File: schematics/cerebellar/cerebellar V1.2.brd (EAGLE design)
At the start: 95.7 x 90.5 mm, 74 parts, among them CON1 ODRV2, CON2 ODRV1, CON3 ODRV3, CON4 ODRV4, CON5 ODRV5, CON6 ODRV6, IC3 LTC7001, K1 PIN20X2, P1 Foot1, P11 Foot2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

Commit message: restart ODrive
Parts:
- U$6: device TS2509:TSSOP-8 -> TS2509:SO08
- moved U2 2.54 mm to (22.5, 52.1)
- moved IC3 2.27 mm to (35.7, 52.1)
- moved R15 2.27 mm to (47.1, 52.1)
- moved R4 2.27 mm to (44.6, 52.1)
- moved R9 2.27 mm to (49.7, 52.1)
- moved C19 2.27 mm to (31.9, 52.1)
- moved R5 2.27 mm to (26.2, 52.1)
- moved R10 2.27 mm to (42.0, 52.1)
- moved R2 2.27 mm to (28.7, 52.1)
- moved R7 2.27 mm to (39.5, 52.1)
- moved C1 2.17 mm to (54.6, 52.1)
- moved R6 2.09 mm to (52.1, 52.1)
- moved U$6 0.76 mm to (34.8, 37.3), turned to 0 degrees
- moved R11 0.57 mm to (50.3, 37.1)
- moved C26 0.57 mm to (27.3, 40.6)
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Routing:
- net N$17: track 73.7 -> 108.1 mm, vias 3 -> 0
- net SENS3: track 115.1 -> 89.1 mm, vias 4 -> 3
- net +5V: track 231.8 -> 257.1 mm, vias 3 -> 0
- net SENS4: track 124.1 -> 99.9 mm, vias 1 -> 2
- net CS: track 68.2 -> 45.8 mm, vias 4 -> 2
- net O2_TX: track 50.8 -> 67.9 mm, vias 1 -> 0
- net SWTCH: track 79.1 -> 92.7 mm, vias 0 -> 1
- net O4_RX: track 38.9 -> 50.7 mm
- net LED_PWM: track 70.8 -> 81.4 mm, vias 3 -> 1
- net T3.3V: track 34.0 -> 44.4 mm, vias 2 -> 4
- net O6_RX: track 64.2 -> 54.0 mm
- net GND: track 539.9 -> 531.6 mm, vias 1 -> 2
- net N$22: track 76.8 -> 83.6 mm, vias 2 -> 3
- net O1_RX: track 78.1 -> 83.1 mm, vias 1 -> 0
- net N$46: track 18.6 -> 22.5 mm
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
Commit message: Ordered PCB V1.2
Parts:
- removed D3: Z 5.1V 1A, diode:DO41Z10
- added LED2: uC, adafruit:LED3MM
- added R12: 1K, rcl:0204/7
- C19: value 1uF, 63V -> 1uF
- moved C1 14.2 mm to (40.4, 52.1)
- moved R4 7.37 mm to (51.9, 52.3)
- moved R13 7.27 mm to (47.0, 35.6), turned to 180 degrees
- moved R11 7.16 mm to (47.0, 43.4), turned to 0 degrees
- moved R7 6.86 mm to (46.4, 52.3)
- moved R20 6.12 mm to (47.0, 33.0), turned to 180 degrees
- moved R6 5.85 mm to (57.9, 52.3)
- moved R9 5.34 mm to (55.0, 52.3)
- moved R8 3.84 mm to (47.0, 40.9), turned to 180 degrees
- moved L2 3.64 mm to (58.0, 37.6)
- moved U$6 2.90 mm to (37.1, 39.1)
- moved R21 2.22 mm to (47.0, 38.2), turned to 0 degrees
- moved U$5 2.09 mm to (50.4, 77.3)
- moved R15 2.05 mm to (49.1, 52.3)
- moved LED1 1.70 mm to (63.9, 57.5)
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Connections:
- net MISO renamed MISO/DC
- new net N$3: LED2.K, R12.1
- new net N$4: LED2.A, U$1.33-MCLK2
- new net RASP_INT: K1.7, U$1.2-OUT2
- net +5V: no longer D3.C
- net GND: now also R12.2; no longer D3.A
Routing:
- net LED_PWM: track 81.4 -> 116.7 mm, vias 1 -> 2
- net N$17: track 108.1 -> 75.6 mm, vias 0 -> 1
- net RASP_INT: track 0.00 -> 31.4 mm, vias 0 -> 2
- net MAG_SCL: track 59.8 -> 87.9 mm
- net +5V: track 257.1 -> 282.7 mm, vias 0 -> 1
- net N$4: track 0.00 -> 19.3 mm
- net GND: track 531.6 -> 514.3 mm, vias 2 -> 3
- net T3.3V: track 44.4 -> 61.6 mm
- net CS: track 45.8 -> 61.2 mm, vias 2 -> 1
- net MAG_SDA: track 67.1 -> 52.6 mm, vias 3 -> 1
- net N$22: track 83.6 -> 69.6 mm, vias 3 -> 4
- net SW: track 37.8 -> 25.7 mm, vias 0 -> 1
- net N$10: track 10.4 -> 21.2 mm
- net O4_RX: track 50.7 -> 40.1 mm
- net TS: track 47.8 -> 38.0 mm
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
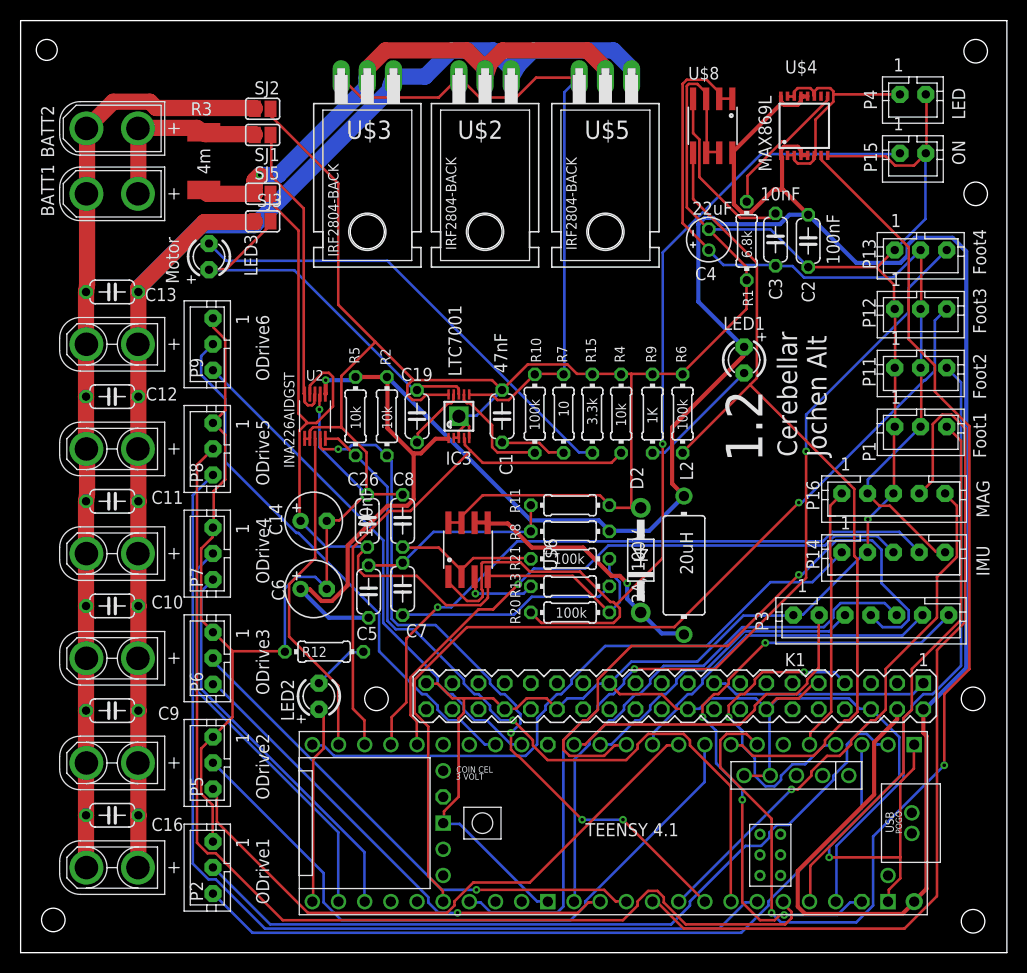
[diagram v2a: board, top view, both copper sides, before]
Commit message: Display is now connected to Raspi instead of Teensy
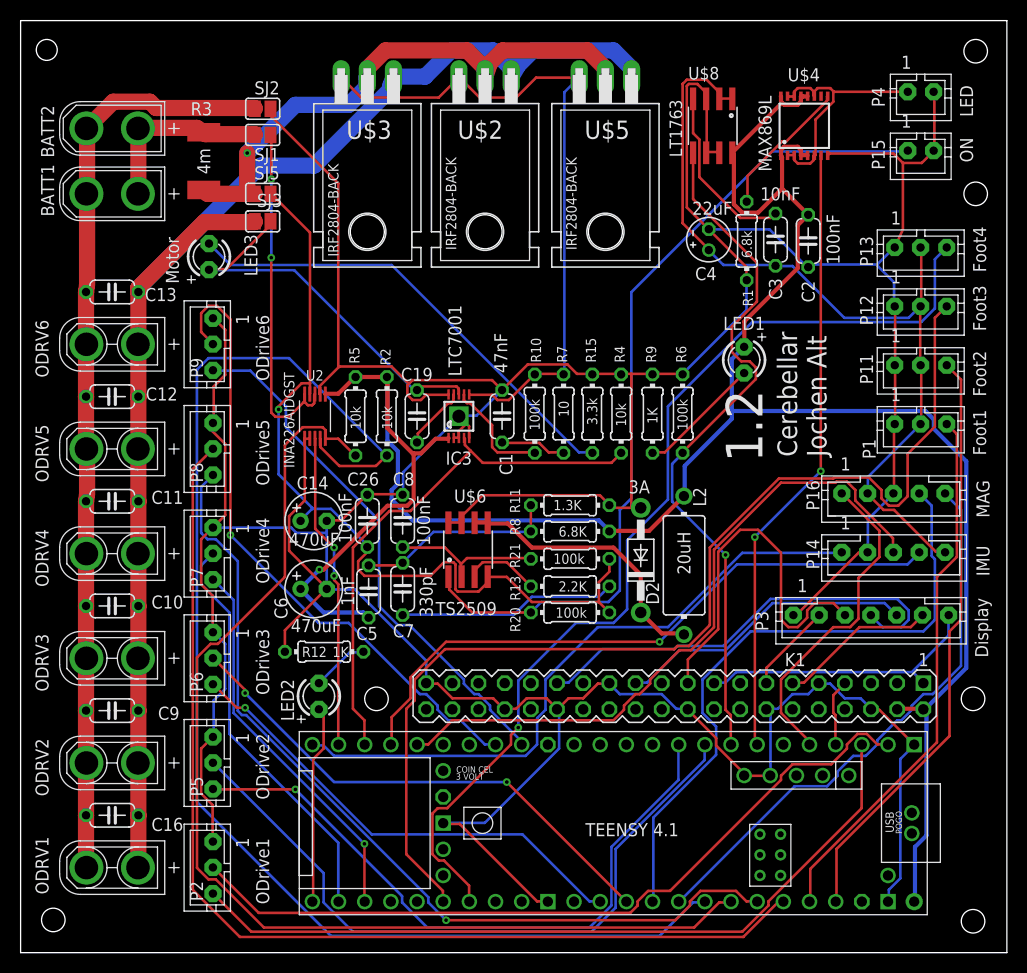
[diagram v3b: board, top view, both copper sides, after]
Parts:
- D2: value 2A, 100V -> 3A
- moved P15 0.80 mm to (81.0, 77.9)
- moved P4 0.80 mm to (81.0, 83.6)
- moved P11 0.25 mm to (81.0, 55.5)
- moved P13 0.25 mm to (81.0, 66.9)
- moved P1 0.25 mm to (81.0, 49.8)
- moved P12 0.25 mm to (81.0, 61.2)
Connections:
- removed net CS: P3.4, U$1.10-CS\MQSR
- removed net MISO/DC: P3.2, U$1.12-MISO/MQSL
- removed net MOSI: P3.3, U$1.11-MOSI/CTX1
- removed net RESET: P3.6, U$1.9-OUT1C
- removed net SCK: P3.5, U$1.13-SCK/LED
- removed net T3.3V: P3.7, U$1.3V3-3
- new net R_CLK: K1.23, P3.5
- new net R_CS/GPIO27: K1.11, P3.6
- new net R_DC/GPIO22: K1.13, P3.2
- new net R_MOSI: K1.19, P3.3
- new net R_RST/GPIO5: K1.29, P3.4
- net 3.3V_RASPI: now also P3.7
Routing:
- net T3.3V: track 61.6 -> 0.00 mm, vias 4 -> 0
- net CS: track 61.2 -> 0.00 mm, vias 1 -> 0
- net N$22: track 69.6 -> 129.4 mm, vias 4 -> 0
- net LED_PWM: track 116.7 -> 59.9 mm
- net +5V: track 282.7 -> 228.0 mm
- net SCK: track 53.0 -> 0.00 mm
- net R_RST/GPIO5: track 0.00 -> 43.4 mm
- net R_MOSI: track 0.00 -> 36.8 mm
- net N$17: track 75.6 -> 109.5 mm, vias 1 -> 0
- net RESET: track 32.6 -> 0.00 mm
- net MISO/DC: track 32.5 -> 0.00 mm
- net MOSI: track 29.5 -> 0.00 mm
- net R_CLK: track 0.00 -> 29.1 mm
- net MAG_SCL: track 87.9 -> 62.5 mm
- net RASP_INT: track 31.4 -> 6.53 mm, vias 2 -> 0
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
